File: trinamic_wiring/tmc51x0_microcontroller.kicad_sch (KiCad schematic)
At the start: 3 parts, among them M4 Stepper_Motor_QSH2818-32-07-0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

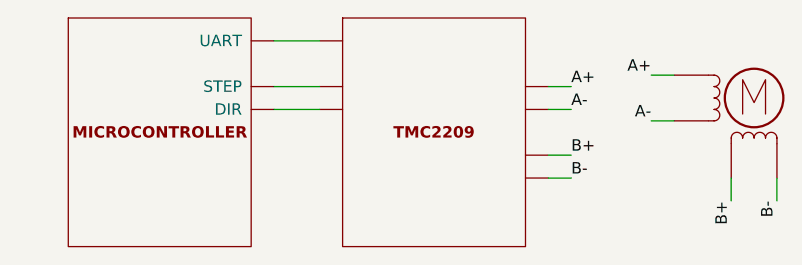
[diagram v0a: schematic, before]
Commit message: Remove unused sheets
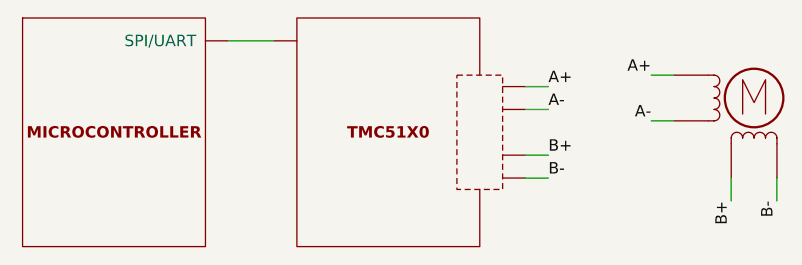
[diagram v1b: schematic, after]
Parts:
- removed TMC14: DOC_TMC2209, symbol Janelia:DOC_TMC2209
- added TMC51X2: TMC51X0_DOC, symbol Janelia:TMC51X0_DOC
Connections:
- net A+: now also TMC51X2.5 (OA1)
- net A-: now also TMC51X2.6 (OA2)
- net B+: now also TMC51X2.7 (OB1)
- net B-: now also TMC51X2.8 (OB2)
- net at MICROCONTROLLER8.1 (SPI/UART): now also TMC51X2.0 (SPI/UART)
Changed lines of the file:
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@@
   (title_block
     (title "Trinamic Wiring")
-    (date "2023-08-02")
-    (rev "0.4")
+    (date "2024-01-31")
+    (rev "0.5")
     (company "Janelia Research Campus")
   )
-  (wire (pts (xy 149.86 93.98) (xy 147.32 93.98))
+  (wire (pts (xy 147.32 93.98) (xy 144.78 93.98))
     (stroke (width 0) (type default))
   )
-  (wire (pts (xy 116.84 81.28) (xy 121.92 81.28))
+  (wire (pts (xy 111.76 81.28) (xy 116.84 81.28))
+    (stroke (width 0) (type default))
+  )
+  (wire (pts (xy 147.32 86.36) (xy 144.78 86.36))
+    (stroke (width 0) (type default))
+  )
+  (wire (pts (xy 147.32 88.9) (xy 144.78 88.9))
     (stroke (width 0) (type default))
   )
@@
     (stroke (width 0) (type default))
   )
-  (wire (pts (xy 149.86 96.52) (xy 147.32 96.52))
-    (stroke (width 0) (type default))
-  )
   (wire (pts (xy 158.75 90.17) (xy 161.29 90.17))
     (stroke (width 0) (type default))
   )
-  (wire (pts (xy 116.84 88.9) (xy 121.92 88.9))
-    (stroke (width 0) (type default))
-  )
-  (wire (pts (xy 149.86 86.36) (xy 147.32 86.36))
+  (wire (pts (xy 147.32 96.52) (xy 144.78 96.52))
     (stroke (width 0) (type default))
   )
@@
     (stroke (width 0) (type default))
   )
-  (wire (pts (xy 116.84 86.36) (xy 121.92 86.36))
-    (stroke (width 0) (type default))
-  )
   (wire (pts (xy 167.64 99.06) (xy 167.64 96.52))
     (stroke (width 0) (type default))
   )
-  (wire (pts (xy 149.86 88.9) (xy 147.32 88.9))
-    (stroke (width 0) (type default))
-  )
-  (label "A-" (at 149.86 88.9 0) (fields_autoplaced)
-    (effects (font (size 1.27 1.27)) (justify left bottom))
-  )
-  (label "A+" (at 149.86 86.36 0) (fields_autoplaced)
-    (effects (font (size 1.27 1.27)) (justify left bottom))
-  )
-  (label "B+" (at 149.86 93.98 0) (fields_autoplaced)
+  (label "A-" (at 147.32 88.9 0) (fields_autoplaced)
     (effects (font (size 1.27 1.27)) (justify left bottom))
   )
@@
     (effects (font (size 1.27 1.27)) (justify right bottom))
   )
-  (label "B-" (at 149.86 96.52 0) (fields_autoplaced)
+  (label "B+" (at 147.32 93.98 0) (fields_autoplaced)
+    (effects (font (size 1.27 1.27)) (justify left bottom))
+  )
+  (label "A+" (at 147.32 86.36 0) (fields_autoplaced)
+    (effects (font (size 1.27 1.27)) (justify left bottom))
+  )
+  (label "B-" (at 147.32 96.52 0) (fields_autoplaced)
     (effects (font (size 1.27 1.27)) (justify left bottom))
   )
@@
     (instances
       (project "trinamic_wiring"
-        (path "/e4144788-6304-493f-818e-5d881d3b7418/c8eda2b5-ab13-4033-82d9-875c9fcaf884/8b14fa14-b5a5-4a20-b7f5-9504bcb63f71"
-          (reference "M4") (unit 1)
-        )
         (path "/e4144788-6304-493f-818e-5d881d3b7418/a161638e-a96f-4455-865a-1d7502675f43/8b14fa14-b5a5-4a20-b7f5-9504bcb63f71"
           (reference "M4") (unit 1)
@@
     )
   )
-  (symbol (lib_id "Janelia:DOC_TMC2209") (at 134.62 91.44 0) (unit 1)
+  (symbol (lib_id "Janelia:DOC_MCU") (at 99.06 91.44 0) (unit 1)
     (in_bom yes) (on_board yes) (dnp no) (fields_autoplaced)
-    (property "Reference" "TMC14" (at 134.62 72.39 0)
+    (property "Reference" "MICROCONTROLLER8" (at 99.06 72.39 0)
       (effects (font (size 1.27 1.27)) hide)
     )
-    (property "Value" "DOC_TMC2209" (at 134.62 77.47 0)
+    (property "Value" "DOC_MCU" (at 99.06 77.47 0)
       (effects (font (size 1.524 1.524)) hide)
     )
-    (property "Footprint" "" (at 132.08 118.11 0)
+    (property "Footprint" "" (at 96.52 118.11 0)
       (effects (font (size 1.524 1.524)) hide)
     )
-    (property "Datasheet" "" (at 134.62 91.44 0)
+    (property "Datasheet" "" (at 99.06 91.44 0)
       (effects (font (size 1.524 1.524)) hide)
     )
-    (property "Sim.Enable" "0" (at 134.62 74.93 0)
-      (effects (font (size 1.27 1.27)) hide)
-    )
-    (pin "0")
-    (pin "1")
-    (pin "10")
-    (pin "2")
-    (pin "3")
-    (pin "4")
-    (pin "5")
-    (pin "6")
-    (pin "7")
-    (pin "8")
-    (pin "9")
-    (instances
-      (project "trinamic_wiring"
-        (path "/e4144788-6304-493f-818e-5d881d3b7418/c8eda2b5-ab13-4033-82d9-875c9fcaf884/8b14fa14-b5a5-4a20-b7f5-9504bcb63f71"
-          (reference "TMC14") (unit 1)
-        )
-        (path "/e4144788-6304-493f-818e-5d881d3b7418/a161638e-a96f-4455-865a-1d7502675f43/8b14fa14-b5a5-4a20-b7f5-9504bcb63f71"
-          (reference "TMC14") (unit 1)
-        )
-      )
-    )
-  )
-  (symbol (lib_id "Janelia:DOC_MCU") (at 104.14 91.44 0) (unit 1)
-    (in_bom yes) (on_board yes) (dnp no) (fields_autoplaced)
-    (property "Reference" "MICROCONTROLLER8" (at 104.14 72.39 0)
-      (effects (font (size 1.27 1.27)) hide)
-    )
-    (property "Value" "DOC_MCU" (at 104.14 77.47 0)
-      (effects (font (size 1.524 1.524)) hide)
-    )
-    (property "Footprint" "" (at 101.6 118.11 0)
-      (effects (font (size 1.524 1.524)) hide)
-    )
-    (property "Datasheet" "" (at 104.14 91.44 0)
-      (effects (font (size 1.524 1.524)) hide)
-    )
-    (property "Sim.Enable" "0" (at 104.14 74.93 0)
+    (property "Sim.Enable" "0" (at 99.06 74.93 0)
       (effects (font (size 1.27 1.27)) hide)
     )
@@
     (instances
       (project "trinamic_wiring"
-        (path "/e4144788-6304-493f-818e-5d881d3b7418/c8eda2b5-ab13-4033-82d9-875c9fcaf884/8b14fa14-b5a5-4a20-b7f5-9504bcb63f71"
-          (reference "MICROCONTROLLER8") (unit 1)
-        )
         (path "/e4144788-6304-493f-818e-5d881d3b7418/a161638e-a96f-4455-865a-1d7502675f43/8b14fa14-b5a5-4a20-b7f5-9504bcb63f71"
           (reference "MICROCONTROLLER8") (unit 1)
         )
       )
+    )
+  )
+  (symbol (lib_id "Janelia:TMC51X0_DOC") (at 129.54 91.44 0) (unit 1)
+    (in_bom yes) (on_board yes) (dnp no) (fields_autoplaced)
+    (property "Reference" "TMC51X2" (at 129.54 72.39 0)
+      (effects (font (size 1.27 1.27)) hide)
+    )
+    (property "Value" "TMC51X0_DOC" (at 129.54 77.47 0)
+      (effects (font (size 1.524 1.524)) hide)
+    )
+    (property "Footprint" "" (at 127 118.11 0)
+      (effects (font (size 1.524 1.524)) hide)
+    )
+    (property "Datasheet" "" (at 129.54 91.44 0)
+      (effects (font (size 1.524 1.524)) hide)
+    )
+    (property "Sim.Enable" "0" (at 129.54 74.93 0)
+      (effects (font (size 1.27 1.27)) hide)
+    )
+    (pin "8")
+    (pin "10")
+    (pin "9")
+    (pin "7")
+    (pin "6")
+    (pin "5")
+    (pin "1")
+    (pin "3")
+    (pin "4")
+    (pin "2")
+    (pin "0")
+    (instances
+      (project "trinamic_wiring"
+        (path "/e4144788-6304-493f-818e-5d881d3b7418/a161638e-a96f-4455-865a-1d7502675f43/8b14fa14-b5a5-4a20-b7f5-9504bcb63f71"
+          (reference "TMC51X2") (unit 1)
+        )
+      )
